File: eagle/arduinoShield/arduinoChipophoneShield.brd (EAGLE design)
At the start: 101.6 x 53.3 mm, 29 parts

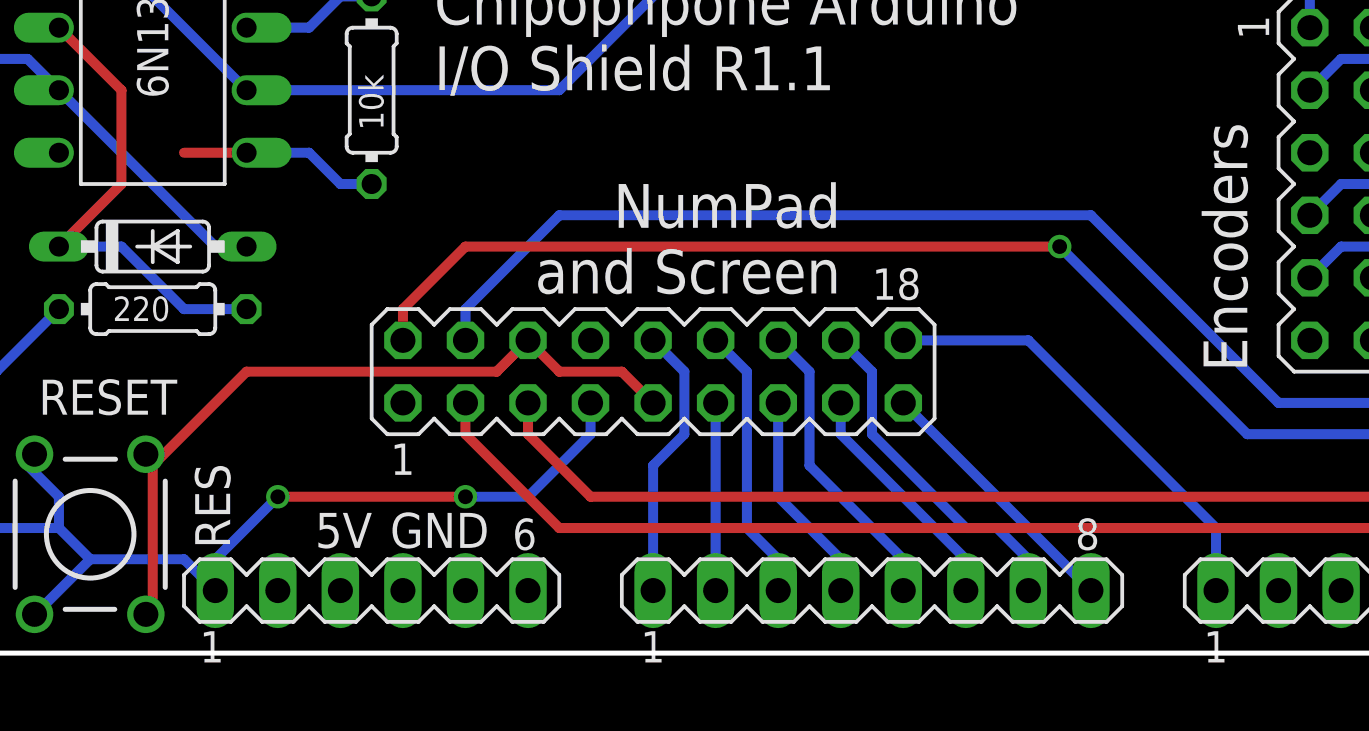
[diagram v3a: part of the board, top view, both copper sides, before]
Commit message: Updated to R1.2, which fixes the missing Pin on the screen header. Also has CS connected now too
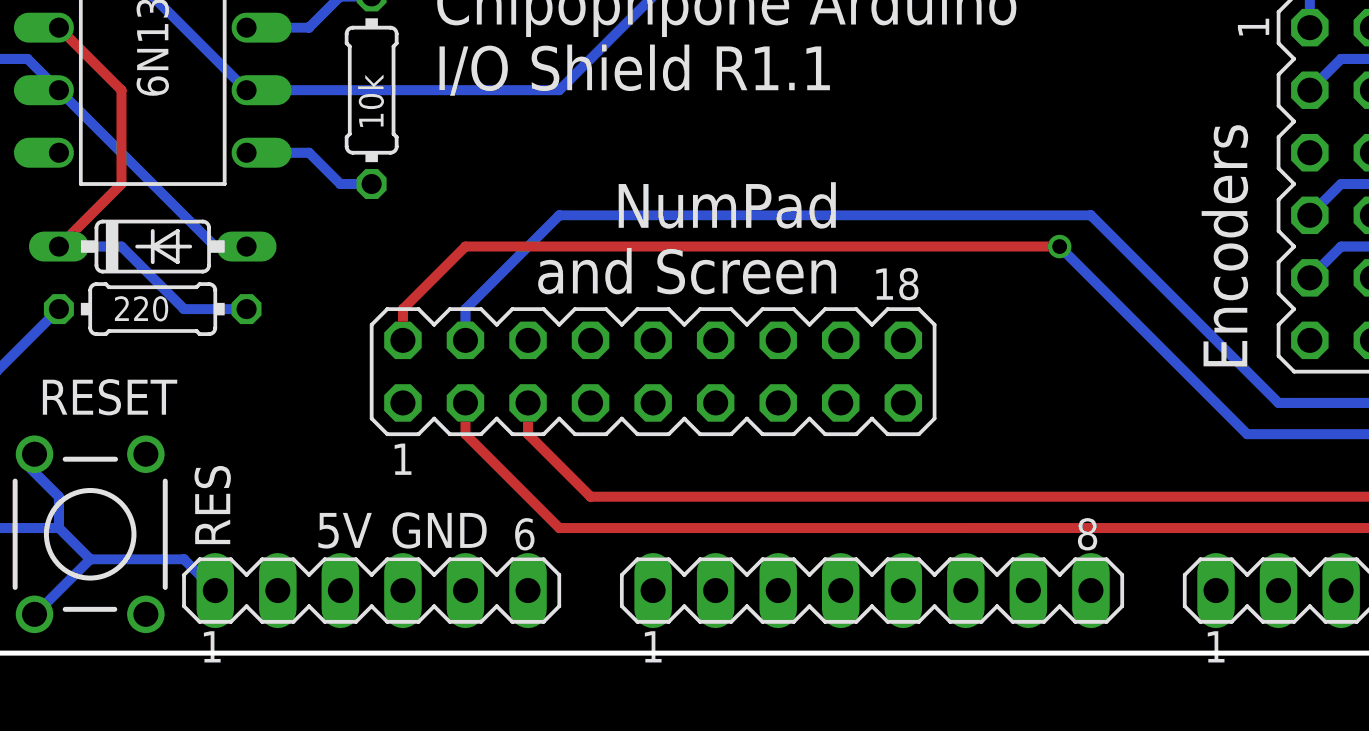
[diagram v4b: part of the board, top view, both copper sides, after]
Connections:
- net 5V: now also SCREEN_NUMPAD.9; no longer SCREEN_NUMPAD.8
- net A0: now also SCREEN_NUMPAD.11; no longer SCREEN_NUMPAD.10
- net A1: now also SCREEN_NUMPAD.12; no longer SCREEN_NUMPAD.11
- net A2: now also SCREEN_NUMPAD.13; no longer SCREEN_NUMPAD.12
- net A3: now also SCREEN_NUMPAD.14; no longer SCREEN_NUMPAD.13
- net A4: now also SCREEN_NUMPAD.15; no longer SCREEN_NUMPAD.14
- net A5: now also SCREEN_NUMPAD.16; no longer SCREEN_NUMPAD.15
- net A6: now also SCREEN_NUMPAD.17; no longer SCREEN_NUMPAD.16
- net A7: now also SCREEN_NUMPAD.18; no longer SCREEN_NUMPAD.17
- net A8: no longer SCREEN_NUMPAD.18
- net D48: now also SCREEN_NUMPAD.6
- net D49: now also SCREEN_NUMPAD.7
- net GND: now also SCREEN_NUMPAD.10; no longer SCREEN_NUMPAD.6, SCREEN_NUMPAD.9
- net RES: now also SCREEN_NUMPAD.8; no longer SCREEN_NUMPAD.7
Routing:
- net GND: track 38.0 -> 5.61 mm
- net RES: track 36.5 -> 17.9 mm, vias 2 -> 0
- net A8: track 18.4 -> 0.00 mm
- net A6: track 14.1 -> 2.54 mm
- net A0: track 11.2 -> 0.00 mm
- net A4: track 12.3 -> 1.27 mm
- net A7: track 10.8 -> 0.00 mm
- net A2: track 11.2 -> 1.27 mm
- net A5: track 9.72 -> 1.27 mm
- net A1: track 7.62 -> 0.00 mm
- net A3: track 8.67 -> 1.27 mm
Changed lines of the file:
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@@
 <contactref element="S1" pad="4"/>
 <contactref element="S1" pad="3"/>
-<contactref element="SCREEN_NUMPAD" pad="7"/>
-<wire x1="48.26" y1="10.16" x2="48.26" y2="8.89" width="0.4064" layer="16"/>
-<wire x1="48.26" y1="8.89" x2="45.72" y2="6.35" width="0.4064" layer="16"/>
-<wire x1="45.72" y1="6.35" x2="43.18" y2="6.35" width="0.4064" layer="16"/>
-<via x="43.18" y="6.35" extent="1-16" drill="0.6" shape="square"/>
-<wire x1="43.18" y1="6.35" x2="35.56" y2="6.35" width="0.4064" layer="1"/>
-<via x="35.56" y="6.35" extent="1-16" drill="0.6" shape="square"/>
-<wire x1="33.02" y1="3.81" x2="35.56" y2="6.35" width="0.4064" layer="16"/>
 <contactref element="SV2" pad="1"/>
 <wire x1="33.02" y1="2.54" x2="31.75" y2="3.81" width="0.4064" layer="16"/>
@@
 <wire x1="26.67" y1="5.08" x2="26.67" y2="6.35" width="0.4064" layer="16"/>
 <wire x1="26.67" y1="6.35" x2="25.4" y2="7.62" width="0.4064" layer="16"/>
-<wire x1="33.02" y1="2.54" x2="33.02" y2="3.81" width="0" layer="19" extent="16-16"/>
+<contactref element="SCREEN_NUMPAD" pad="8"/>
+<wire x1="33.02" y1="2.54" x2="48.26" y2="12.7" width="0" layer="19" extent="1-1"/>
 <wire x1="22.86" y1="5.461" x2="22.86" y2="5.08" width="0" layer="19" extent="16-16"/>
 <wire x1="25.6794" y1="1.5748" x2="25.4" y2="1.27" width="0" layer="19" extent="16-16"/>
@@
 <contactref element="LED" pad="1"/>
 <contactref element="SCREEN_NUMPAD" pad="1"/>
-<contactref element="SCREEN_NUMPAD" pad="8"/>
 <contactref element="SV2" pad="3"/>
 <contactref element="OK1" pad="8"/>
@@
 <vertex x="96.52" y="53.34"/>
 </polygon>
+<contactref element="SCREEN_NUMPAD" pad="9"/>
 </signal>
 <signal name="GND">
@@
 <contactref element="S1" pad="2"/>
 <contactref element="LED1" pad="K"/>
-<contactref element="SCREEN_NUMPAD" pad="6"/>
-<contactref element="SCREEN_NUMPAD" pad="9"/>
-<wire x1="30.48" y1="7.62" x2="30.48" y2="1.27" width="0.4064" layer="1"/>
-<wire x1="45.72" y1="12.7" x2="44.45" y2="11.43" width="0.4064" layer="1"/>
-<wire x1="45.72" y1="12.7" x2="46.99" y2="11.43" width="0.4064" layer="1"/>
-<wire x1="46.99" y1="11.43" x2="49.53" y2="11.43" width="0.4064" layer="1"/>
-<wire x1="49.53" y1="11.43" x2="50.8" y2="10.16" width="0.4064" layer="1"/>
-<wire x1="30.48" y1="7.62" x2="34.29" y2="11.43" width="0.4064" layer="1"/>
-<wire x1="34.29" y1="11.43" x2="44.45" y2="11.43" width="0.4064" layer="1"/>
 <contactref element="JP3" pad="7"/>
 <contactref element="SV2" pad="4"/>
@@
 <wire x1="36.83" y1="20.32" x2="38.1" y2="19.05" width="0.4064" layer="16"/>
 <wire x1="38.1" y1="19.05" x2="39.37" y2="19.05" width="0.4064" layer="16"/>
-<wire x1="31.75" y1="20.32" x2="34.29" y2="20.32" width="0.4064" layer="1"/>
 <contactref element="MIDI_OUT" pad="1"/>
 <contactref element="MIDI_IN" pad="1"/>
@@
 <contactref element="ENCODERS" pad="11"/>
 <contactref element="PUSHBUTTONS" pad="1"/>
+<contactref element="SCREEN_NUMPAD" pad="10"/>
 </signal>
 <signal name="A0">
-<contactref element="SCREEN_NUMPAD" pad="10"/>
-<wire x1="50.8" y1="2.54" x2="50.8" y2="7.62" width="0.4064" layer="16"/>
-<wire x1="50.8" y1="7.62" x2="52.07" y2="8.89" width="0.4064" layer="16"/>
-<wire x1="52.07" y1="8.89" x2="52.07" y2="11.43" width="0.4064" layer="16"/>
-<wire x1="52.07" y1="11.43" x2="50.8" y2="12.7" width="0.4064" layer="16"/>
 <contactref element="JP1" pad="1"/>
+<contactref element="SCREEN_NUMPAD" pad="11"/>
+<wire x1="50.8" y1="2.54" x2="53.34" y2="10.16" width="0" layer="19" extent="1-1"/>
 </signal>
 <signal name="A1">
-<contactref element="SCREEN_NUMPAD" pad="11"/>
-<wire x1="53.34" y1="10.16" x2="53.34" y2="2.54" width="0.4064" layer="16"/>
 <contactref element="JP1" pad="2"/>
+<contactref element="SCREEN_NUMPAD" pad="12"/>
+<wire x1="53.34" y1="2.54" x2="53.34" y2="12.7" width="0" layer="19" extent="1-1"/>
 </signal>
 <signal name="A2">
-<contactref element="SCREEN_NUMPAD" pad="12"/>
-<wire x1="53.34" y1="12.7" x2="54.61" y2="11.43" width="0.4064" layer="16"/>
-<wire x1="54.61" y1="11.43" x2="54.61" y2="5.08" width="0.4064" layer="16"/>
-<wire x1="54.61" y1="5.08" x2="55.88" y2="3.81" width="0.4064" layer="16"/>
 <wire x1="55.88" y1="3.81" x2="55.88" y2="2.54" width="0.4064" layer="16"/>
 <contactref element="JP1" pad="3"/>
+<contactref element="SCREEN_NUMPAD" pad="13"/>
+<wire x1="55.88" y1="3.81" x2="55.88" y2="10.16" width="0" layer="19" extent="16-16"/>
 </signal>
 <signal name="A3">
-<contactref element="SCREEN_NUMPAD" pad="13"/>
-<wire x1="55.88" y1="10.16" x2="55.88" y2="6.35" width="0.4064" layer="16"/>
-<wire x1="55.88" y1="6.35" x2="58.42" y2="3.81" width="0.4064" layer="16"/>
 <wire x1="58.42" y1="3.81" x2="58.42" y2="2.54" width="0.4064" layer="16"/>
 <contactref element="JP1" pad="4"/>
+<contactref element="SCREEN_NUMPAD" pad="14"/>
+<wire x1="58.42" y1="3.81" x2="55.88" y2="12.7" width="0" layer="19" extent="16-16"/>
 </signal>
 <signal name="A4">
-<contactref element="SCREEN_NUMPAD" pad="14"/>
-<wire x1="55.88" y1="12.7" x2="57.15" y2="11.43" width="0.4064" layer="16"/>
-<wire x1="57.15" y1="11.43" x2="57.15" y2="7.62" width="0.4064" layer="16"/>
-<wire x1="57.15" y1="7.62" x2="60.96" y2="3.81" width="0.4064" layer="16"/>
 <wire x1="60.96" y1="3.81" x2="60.96" y2="2.54" width="0.4064" layer="16"/>
 <contactref element="JP1" pad="5"/>
+<contactref element="SCREEN_NUMPAD" pad="15"/>
+<wire x1="60.96" y1="3.81" x2="58.42" y2="10.16" width="0" layer="19" extent="16-16"/>
 </signal>
 <signal name="A5">
-<contactref element="SCREEN_NUMPAD" pad="15"/>
-<wire x1="58.42" y1="10.16" x2="58.42" y2="8.89" width="0.4064" layer="16"/>
-<wire x1="58.42" y1="8.89" x2="63.5" y2="3.81" width="0.4064" layer="16"/>
 <wire x1="63.5" y1="3.81" x2="63.5" y2="2.54" width="0.4064" layer="16"/>
 <contactref element="JP1" pad="6"/>
+<contactref element="SCREEN_NUMPAD" pad="16"/>
+<wire x1="63.5" y1="3.81" x2="58.42" y2="12.7" width="0" layer="19" extent="16-16"/>
 </signal>
 <signal name="A6">
-<contactref element="SCREEN_NUMPAD" pad="16"/>
-<wire x1="58.42" y1="12.7" x2="59.69" y2="11.43" width="0.4064" layer="16"/>
-<wire x1="59.69" y1="11.43" x2="59.69" y2="8.89" width="0.4064" layer="16"/>
-<wire x1="59.69" y1="8.89" x2="63.5" y2="5.08" width="0.4064" layer="16"/>
 <wire x1="63.5" y1="5.08" x2="64.77" y2="5.08" width="0.4064" layer="16"/>
-<wire x1="64.77" y1="5.08" x2="66.04" y2="3.81" width="0.4064" layer="16"/>
 <wire x1="66.04" y1="3.81" x2="66.04" y2="2.54" width="0.4064" layer="16"/>
 <contactref element="JP1" pad="7"/>
+<contactref element="SCREEN_NUMPAD" pad="17"/>
+<wire x1="63.5" y1="5.08" x2="60.96" y2="10.16" width="0" layer="19" extent="16-16"/>
+<wire x1="66.04" y1="3.81" x2="64.77" y2="5.08" width="0" layer="19" extent="16-16"/>
 </signal>
 <signal name="A7">
-<contactref element="SCREEN_NUMPAD" pad="17"/>
-<wire x1="60.96" y1="10.16" x2="68.58" y2="2.54" width="0.4064" layer="16"/>
 <contactref element="JP1" pad="8"/>
+<contactref element="SCREEN_NUMPAD" pad="18"/>
+<wire x1="68.58" y1="2.54" x2="60.96" y2="12.7" width="0" layer="19" extent="1-1"/>
 </signal>
 <signal name="A8">
-<contactref element="SCREEN_NUMPAD" pad="18"/>
-<wire x1="60.96" y1="12.7" x2="66.04" y2="12.7" width="0.4064" layer="16"/>
-<wire x1="66.04" y1="12.7" x2="73.66" y2="5.08" width="0.4064" layer="16"/>
-<wire x1="73.66" y1="5.08" x2="73.66" y2="2.54" width="0.4064" layer="16"/>
 <contactref element="JP2" pad="1"/>
 </signal>
@@
 <signal name="D48">
 <contactref element="SV1" pad="27"/>
+<contactref element="SCREEN_NUMPAD" pad="6"/>
+<wire x1="45.72" y1="12.7" x2="93.98" y2="15.24" width="0" layer="19" extent="1-1"/>
 </signal>
 <signal name="D41">
@@
 <signal name="D49">
 <contactref element="SV1" pad="28"/>
+<contactref element="SCREEN_NUMPAD" pad="7"/>
+<wire x1="48.26" y1="10.16" x2="96.52" y2="15.24" width="0" layer="19" extent="1-1"/>
 </signal>
 <signal name="3.3">
